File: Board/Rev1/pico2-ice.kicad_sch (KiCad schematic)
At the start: 123 parts, among them J1 USB_C_Receptacle_USB2.0, J2 Conn_02x20_Odd_Even, J3 Conn_02x20_Odd_Even, J5 BM03B-SRSS-TB, J6 SFV22R-2STE1HLF, SW1 CS1213AGF260, SW2 CS1213AGF260, U1 NCP115AMX120TCG, U2 W25Q32JVSSIQ, U3 RP2350_80QFN, U4 TL431DBZ, U5 APS6404L-3SQN-SN, U6 ICE40UP5K-SG48ITR, U8 W25Q32JVSSIQ, U9 NCP115AMX330TCG, Y1 ABM8-272-T3

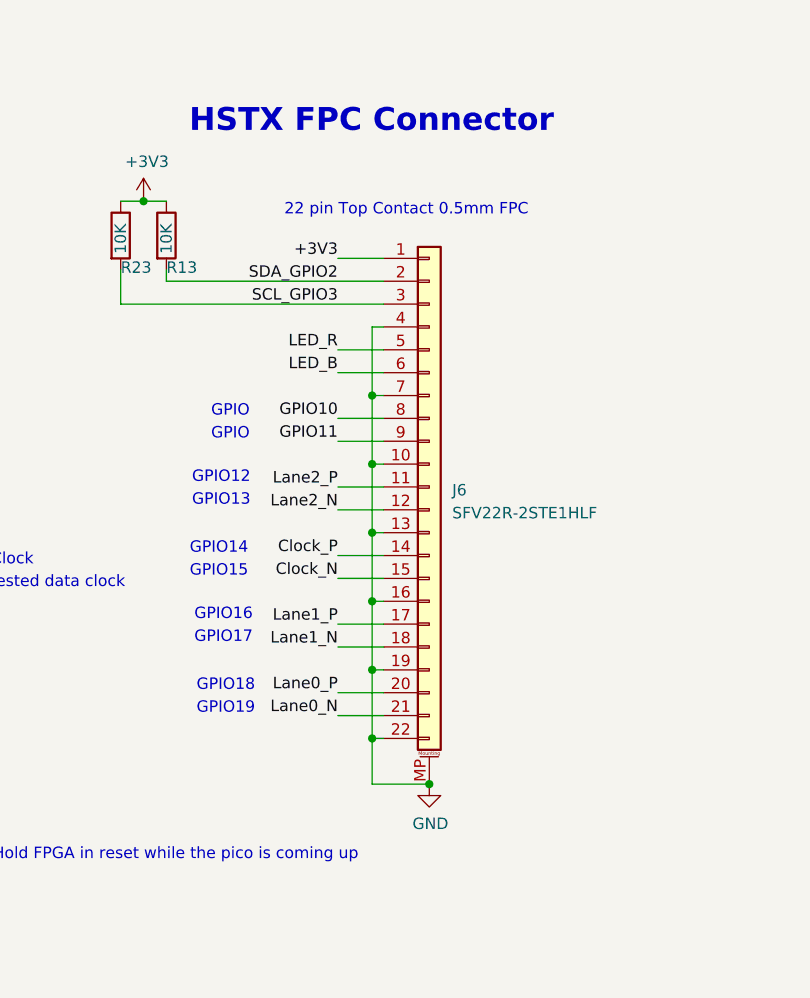
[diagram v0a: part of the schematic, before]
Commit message: Unravelled the HSTX port after changing to a top contact part.
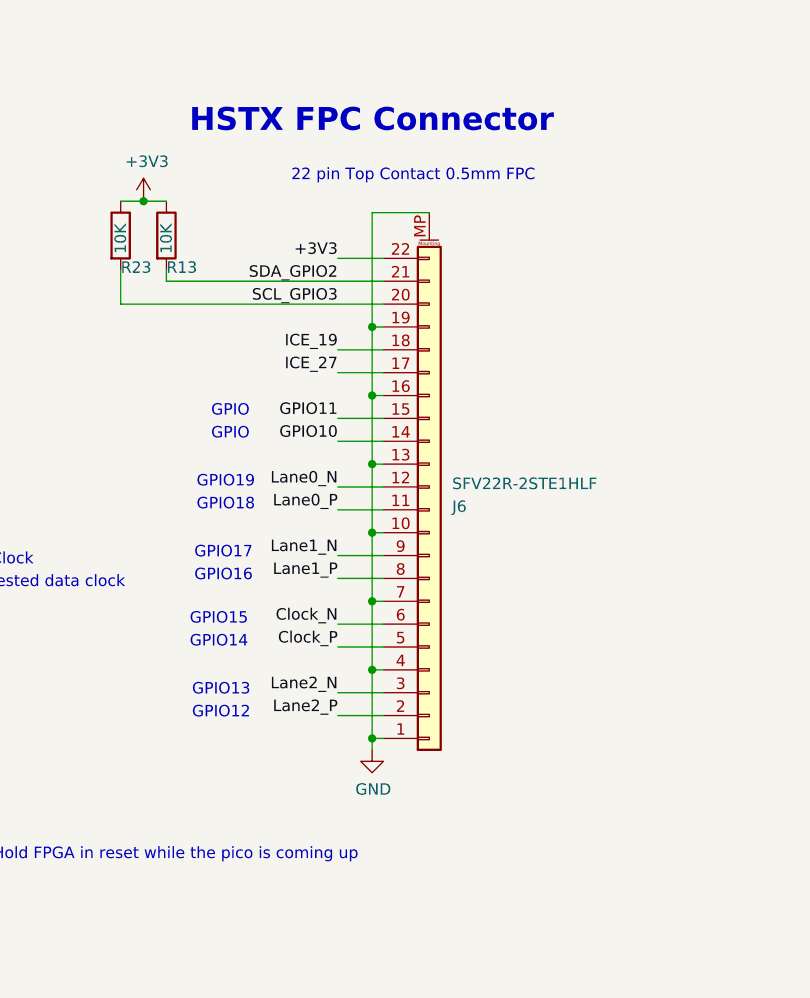
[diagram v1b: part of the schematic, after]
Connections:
- net +3V3: now also J6.22 (Pin_22); no longer J6.1 (Pin_1)
- net Clock_N: now also J6.6 (Pin_6); no longer J6.15 (Pin_15)
- net Clock_P: now also J6.5 (Pin_5); no longer J6.14 (Pin_14)
- net GND: now also J6.1 (Pin_1); no longer J6.22 (Pin_22)
- net GPIO10: now also J6.14 (Pin_14); no longer J6.8 (Pin_8)
- net GPIO11: now also J6.15 (Pin_15); no longer J6.9 (Pin_9)
- net ICE_19: now also J6.18 (Pin_18)
- net ICE_27: now also J6.17 (Pin_17)
- net LED_B: no longer J6.6 (Pin_6)
- net LED_R: no longer J6.5 (Pin_5)
- net Lane0_N: now also J6.12 (Pin_12); no longer J6.21 (Pin_21)
- net Lane0_P: now also J6.11 (Pin_11); no longer J6.20 (Pin_20)
- net Lane1_N: now also J6.9 (Pin_9); no longer J6.18 (Pin_18)
- net Lane1_P: now also J6.8 (Pin_8); no longer J6.17 (Pin_17)
- net Lane2_N: now also J6.3 (Pin_3); no longer J6.12 (Pin_12)
- net Lane2_P: now also J6.2 (Pin_2); no longer J6.11 (Pin_11)
- net SCL_GPIO3: now also J6.20 (Pin_20); no longer J6.3 (Pin_3)
- net SDA_GPIO2: now also J6.21 (Pin_21); no longer J6.2 (Pin_2)

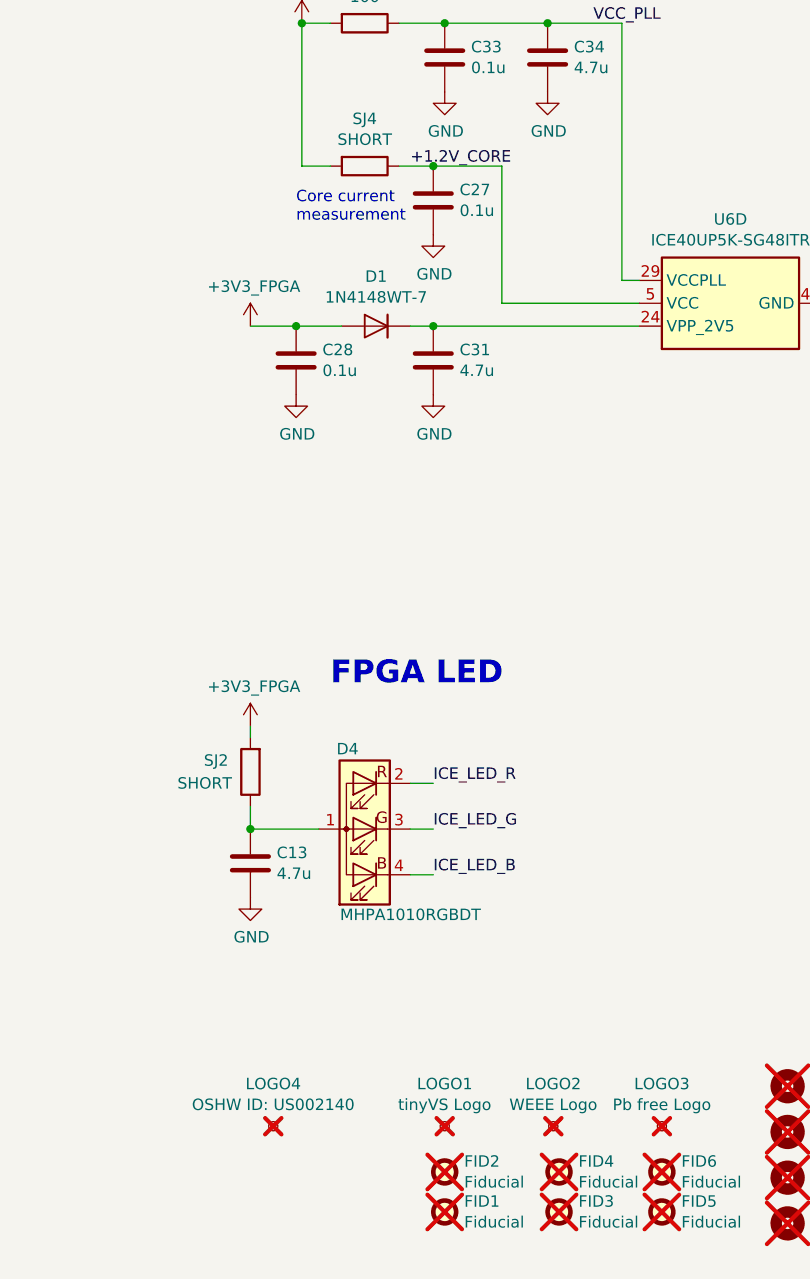
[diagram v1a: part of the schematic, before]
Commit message: Changed loading caps to 10pF, changed HSTX port naming to be consistent with other RPi boards with no routing changes, added docs for FPC connector
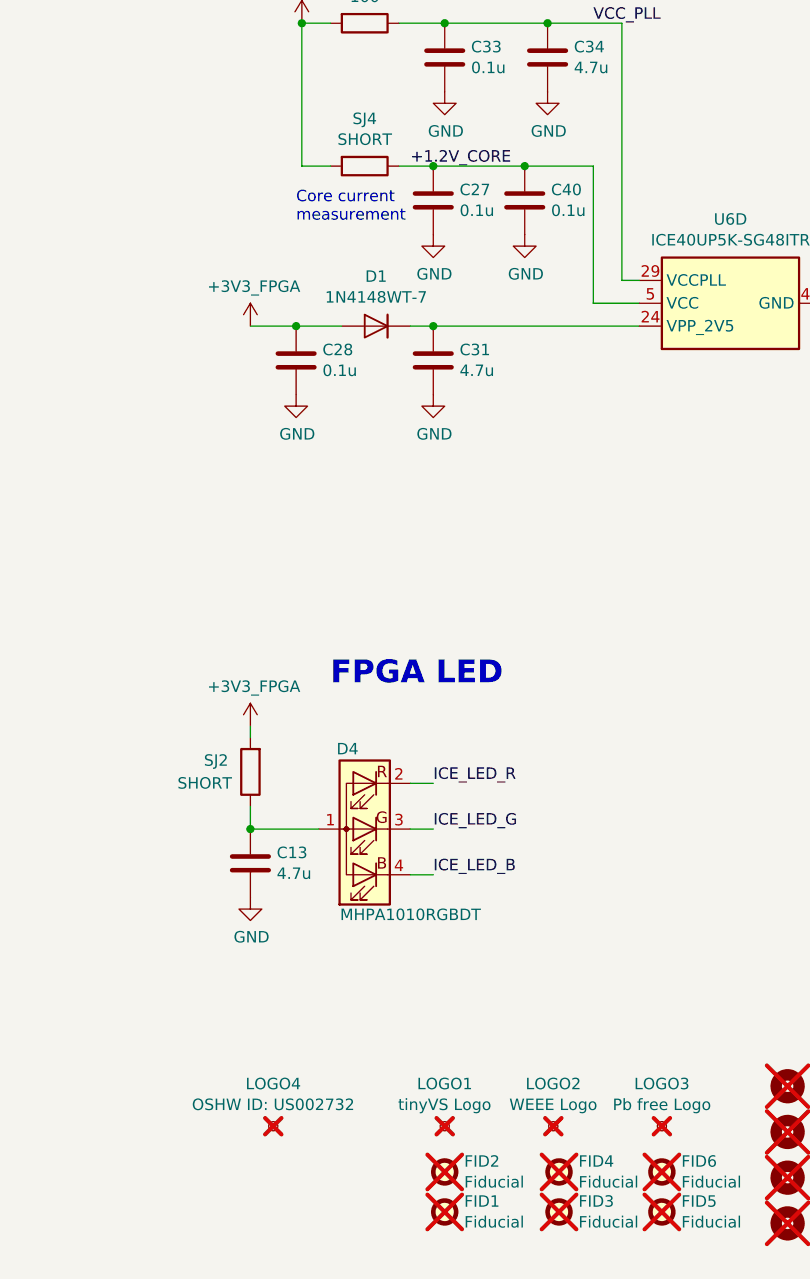
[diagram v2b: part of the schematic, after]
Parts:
- added C40: 0.1u, Capacitor_SMD:C_0402_1005Metric, symbol UPduino_v3.0:Device_C
- LOGO4: value OSHW ID: US002140 -> OSHW ID: US002732
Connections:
- net +1.2V_CORE: now also C40.1
- net GND: now also C40.2
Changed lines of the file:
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@@
 	)
 	(junction
+		(at 425.45 284.48)
+		(diameter 0)
+		(color 0 0 0 0)
+	)
+	(junction
 		(at 227.33 232.41)
 		(diameter 0)
@@
 	(wire
 		(pts
-			(xy 422.91 284.48) (xy 422.91 299.72)
+			(xy 433.07 284.48) (xy 433.07 299.72)
 		)
 		(stroke
@@
 	(wire
 		(pts
-			(xy 422.91 299.72) (xy 438.15 299.72)
+			(xy 433.07 299.72) (xy 438.15 299.72)
 		)
 		(stroke
@@
 	(wire
 		(pts
-			(xy 415.29 284.48) (xy 422.91 284.48)
+			(xy 415.29 284.48) (xy 425.45 284.48)
 		)
 		(stroke
@@
 	(wire
 		(pts
+			(xy 425.45 284.48) (xy 433.07 284.48)
+		)
+		(stroke
+			(width 0)
+			(type default)
+		)
+	)
+	(wire
+		(pts
 			(xy 497.84 275.59) (xy 497.84 278.13)
 		)
@@
 	)
 	(symbol
+		(lib_id "UPduino_v3.0:power_GND")
+		(at 425.45 292.1 0)
+		(unit 1)
+		(exclude_from_sim no)
+		(in_bom yes)
+		(on_board yes)
+		(dnp no)
+		(property "Reference" "#PWR083"
+			(at 425.45 298.45 0)
+			(effects
+				(font
+					(size 1.27 1.27)
+				)
+				(hide yes)
+			)
+		)
+		(property "Value" "GND"
+			(at 425.577 296.4942 0)
+			(effects
+				(font
+					(size 1.27 1.27)
+				)
+			)
+		)
+		(property "Footprint" ""
+			(at 425.45 292.1 0)
+			(effects
+				(font
+					(size 1.27 1.27)
+				)
+				(hide yes)
+			)
+		)
+		(property "Datasheet" ""
+			(at 425.45 292.1 0)
+			(effects
+				(font
+					(size 1.27 1.27)
+				)
+				(hide yes)
+			)
+		)
+		(property "Description" ""
+			(at 425.45 292.1 0)
+			(effects
+				(font
+					(size 1.27 1.27)
+				)
+				(hide yes)
+			)
+		)
+		(pin "1"
+		)
+		(instances
+			(project "pico2-ice"
+				(path "/2ff44921-0562-495a-89f5-ac439f192d90"
+					(reference "#PWR083")
+					(unit 1)
+				)
+			)
+		)
+	)
+	(symbol
 		(lib_id "power:GND")
 		(at 64.77 156.21 0)
@@
 	(symbol
 		(lib_id "UPduino_v3.0:Device_C")
+		(at 425.45 288.29 0)
+		(unit 1)
+		(exclude_from_sim no)
+		(in_bom yes)
+		(on_board yes)
+		(dnp no)
+		(property "Reference" "C40"
+			(at 428.371 287.1216 0)
+			(effects
+				(font
+					(size 1.27 1.27)
+				)
+				(justify left)
+			)
+		)
+		(property "Value" "0.1u"
+			(at 428.371 289.433 0)
+			(effects
+				(font
+					(size 1.27 1.27)
+				)
+				(justify left)
+			)
+		)
+		(property "Footprint" "Capacitor_SMD:C_0402_1005Metric"
+			(at 426.4152 292.1 0)
+			(effects
+				(font
+					(size 1.27 1.27)
+				)
+				(hide yes)
+			)
+		)
+		(property "Datasheet" "~"
+			(at 425.45 288.29 0)
+			(effects
+				(font
+					(size 1.27 1.27)
+				)
+				(hide yes)
+			)
+		)
+		(property "Description" "CAP CER 0.1UF 16V X7R 0402"
+			(at 425.45 288.29 0)
+			(effects
+				(font
+					(size 1.27 1.27)
+				)
+				(hide yes)
+			)
+		)
+		(property "Digi-Key Part Number" ""
+			(at 425.45 288.29 0)
+			(effects
+				(font
+					(size 1.27 1.27)
+				)
+				(hide yes)
+			)
+		)
+		(property "MPN" "GRM155R71C104KA88J"
+			(at 425.45 288.29 0)
+			(effects
+				(font
+					(size 1.27 1.27)
+				)
+				(hide yes)
+			)
+		)
+		(property "Manufacturer" "Murata Electronics"
+			(at 425.45 288.29 0)
+			(effects
+				(font
+					(size 1.27 1.27)
+				)
+				(hide yes)
+			)
+		)
+		(property "Supplier" "Mouser"
+			(at 425.45 288.29 0)
+			(effects
+				(font
+					(size 1.27 1.27)
+				)
+				(hide yes)
+			)
+		)
+		(pin "1"
+		)
+		(pin "2"
+		)
+		(instances
+			(project "pico2-ice"
+				(path "/2ff44921-0562-495a-89f5-ac439f192d90"
+					(reference "C40")
+					(unit 1)
+				)
+			)
+		)
+	)
+	(symbol
+		(lib_id "UPduino_v3.0:Device_C")
 		(at 170.18 116.84 0)
 		(unit 1)
@@
 			)
 		)
-		(property "Value" "OSHW ID: US002140"
+		(property "Value" "OSHW ID: US002732"
 			(at 397.51 388.7724 0)
 			(effects
